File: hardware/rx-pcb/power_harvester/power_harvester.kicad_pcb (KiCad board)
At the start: 4 copper layers, 59 x 46.8 mm, 42 parts, among them J1 Conn_Coaxial_Small, J2 Conn_01x02_Pin, J3 Conn_Coaxial_Small, J4 Conn_Coaxial_Small

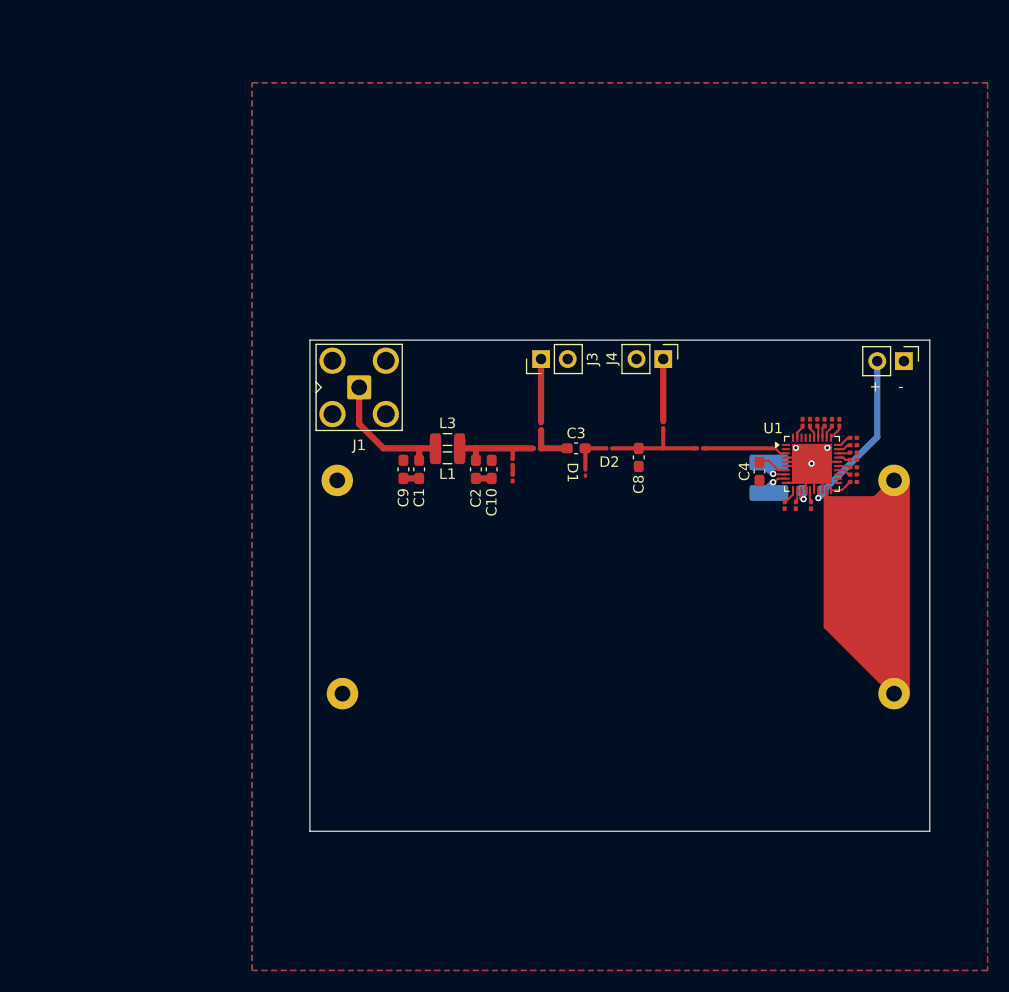
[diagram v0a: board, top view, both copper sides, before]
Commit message: fixed capacitance issue on harvester board
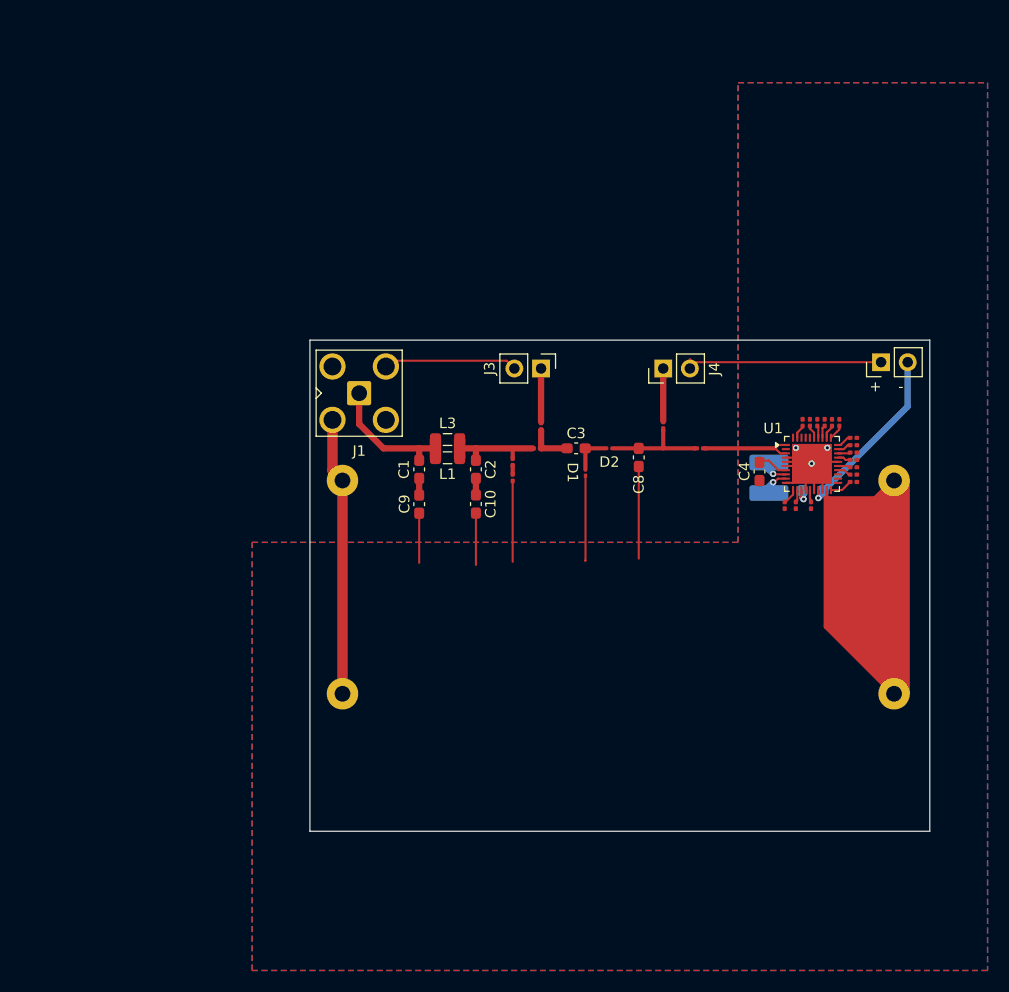
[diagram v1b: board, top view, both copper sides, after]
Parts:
- moved C9 3.64 mm to (106.9, 90.6), turned to -90 degrees
- moved C10 3.62 mm to (112.3, 90.6), turned to -90 degrees
- moved J2 2.18 mm to (150.9, 77.1), turned to 90 degrees
- moved J3 0.90 mm to (118.5, 77.7), turned to -90 degrees
- moved J4 0.90 mm to (130.1, 77.7), turned to 90 degrees
- moved J1 0.55 mm to (101.2, 80.0)
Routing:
- net GND: track 21.9 -> 114.0 mm
- net /Pin: track 7.96 -> 9.10 mm
- net /Po: track 16.3 -> 17.4 mm
- net Net-(J3-In): track 5.99 -> 5.02 mm
- net Net-(J4-In): track 5.89 -> 4.99 mm
- net Net-(J1-In): track 12.8 -> 12.2 mm

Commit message: harvester updates
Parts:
- added R21: x, Resistor_SMD:R_0805_2012Metric_Pad1.20x1.40mm_HandSolder, F.Cu at (152.2, 104.2)
- added R22: x, Resistor_SMD:R_0805_2012Metric_Pad1.20x1.40mm_HandSolder, F.Cu at (152.2, 100.5)
- added R23: x, Resistor_SMD:R_0805_2012Metric_Pad1.20x1.40mm_HandSolder, F.Cu at (152.2, 96.8)
- added R24: x, Resistor_SMD:R_0805_2012Metric_Pad1.20x1.40mm_HandSolder, F.Cu at (152.2, 93.0)
- added R25: x, Resistor_SMD:R_0805_2012Metric_Pad1.20x1.40mm_HandSolder, F.Cu at (139.2, 84.0)
- C1, C10, C2, C9: footprint Capacitor_SMD:C_0603_1608Metric_Pad1.08x0.95mm_HandSolder -> Capacitor_SMD:C_0402_1005Metric_Pad0.74x0.62mm_HandSolder
- moved C9 2.56 mm to (106.9, 88.0)
- moved C10 2.55 mm to (112.3, 88.0)
- moved R11 2.26 mm to (146.8, 90.2), turned to 90 degrees
- moved C2 1.45 mm to (112.3, 85.8)
- moved C1 1.43 mm to (106.9, 85.9)
- moved R19 0.72 mm to (118.5, 83.9)
- moved R14 0.51 mm to (148.8, 87.8)
- moved R4 0.51 mm to (148.8, 87.1)
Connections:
- U1 pad 2: unconnected-(U1-ZMPP-Pad2) -> Net-(U1-ZMPP)
- U1 pad 21: unconnected-(U1-ST_OVDIS-Pad21) -> Net-(U1-ST_OVDIS)
- U1 pad 22: unconnected-(U1-STO_RDY-Pad22) -> Net-(U1-STO_RDY)
- U1 pad 23: unconnected-(U1-STO_OVCH-Pad23) -> Net-(U1-STO_OVCH)
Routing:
- net Net-(U1-ST_OVDIS): track 0.00 -> 17.1 mm
- net /bank: track 49.5 -> 32.7 mm, vias 0 -> 1
- net Net-(U1-STO_RDY): track 0.00 -> 13.8 mm
- net Net-(U1-STO_OVCH): track 0.00 -> 10.6 mm
- net GND: track 114.0 -> 119.8 mm, vias 3 -> 5
- net /Pin: track 9.10 -> 13.0 mm, vias 0 -> 2
- net Net-(U1-ZMPP): track 0.00 -> 2.11 mm
- net Net-(C1-Pad2): track 1.59 -> 0.00 mm
- net Net-(U1-EN_STO_CH): track 2.15 -> 0.99 mm
- net Net-(J1-In): track 12.2 -> 11.1 mm
- net Net-(D3-K): track 9.04 -> 7.90 mm
- net Net-(C3-Pad1): track 3.90 -> 3.01 mm
- net Net-(U1-LOAD_CFG[1]): track 1.19 -> 1.70 mm
- net Net-(C10-Pad1): track 1.58 -> 1.06 mm

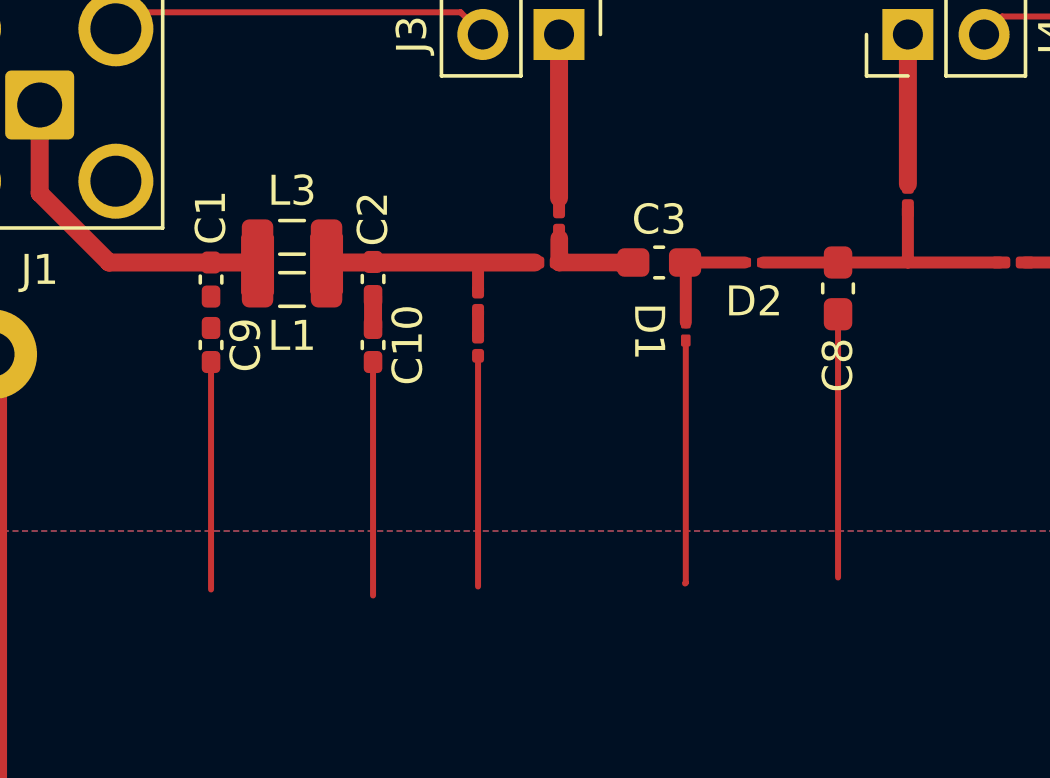
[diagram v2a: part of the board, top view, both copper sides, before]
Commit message: fixed capacitance issue on harvester board
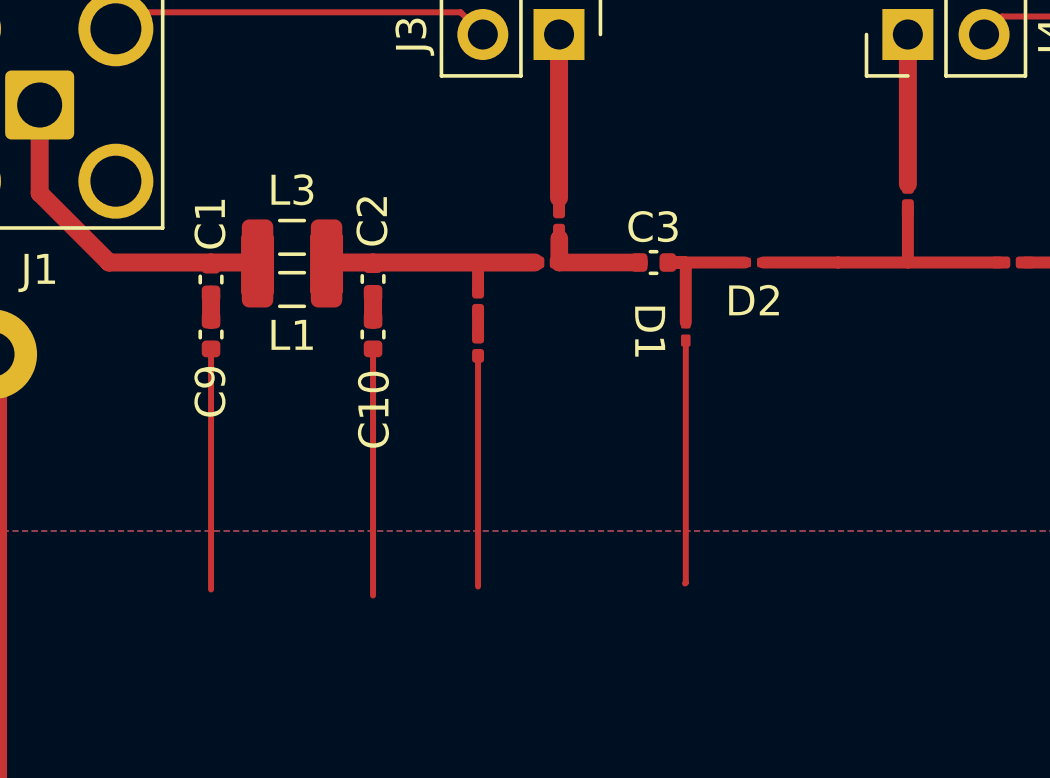
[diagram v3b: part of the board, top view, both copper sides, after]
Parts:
- removed C8: 22u, Capacitor_SMD:C_0603_1608Metric_Pad1.08x0.95mm_HandSolder
- C1, C10, C2, C9: footprint Capacitor_SMD:C_0402_1005Metric_Pad0.74x0.62mm_HandSolder -> Capacitor_SMD:C_0402_1005Metric
- C3: footprint Capacitor_SMD:C_0603_1608Metric_Pad1.08x0.95mm_HandSolder -> Capacitor_SMD:C_0402_1005Metric
- D1, D2: value D -> JDH2S02SL
- D3, D4: value D_Zener -> SP4340L-01WTG
- moved C10 0.35 mm to (112.3, 87.7)
- moved C9 0.35 mm to (106.9, 87.7)
- moved C3 0.19 mm to (121.7, 85.3)
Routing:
- net GND: track 119.8 -> 111.9 mm
- net Net-(D1-K): track 4.01 -> 5.15 mm
- net Net-(C1-Pad2): track 0.00 -> 0.85 mm
- removed copper zone on In1.Cu, net GND
- removed copper zone on In2.Cu, net GND
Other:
- copper layers 4 -> 2

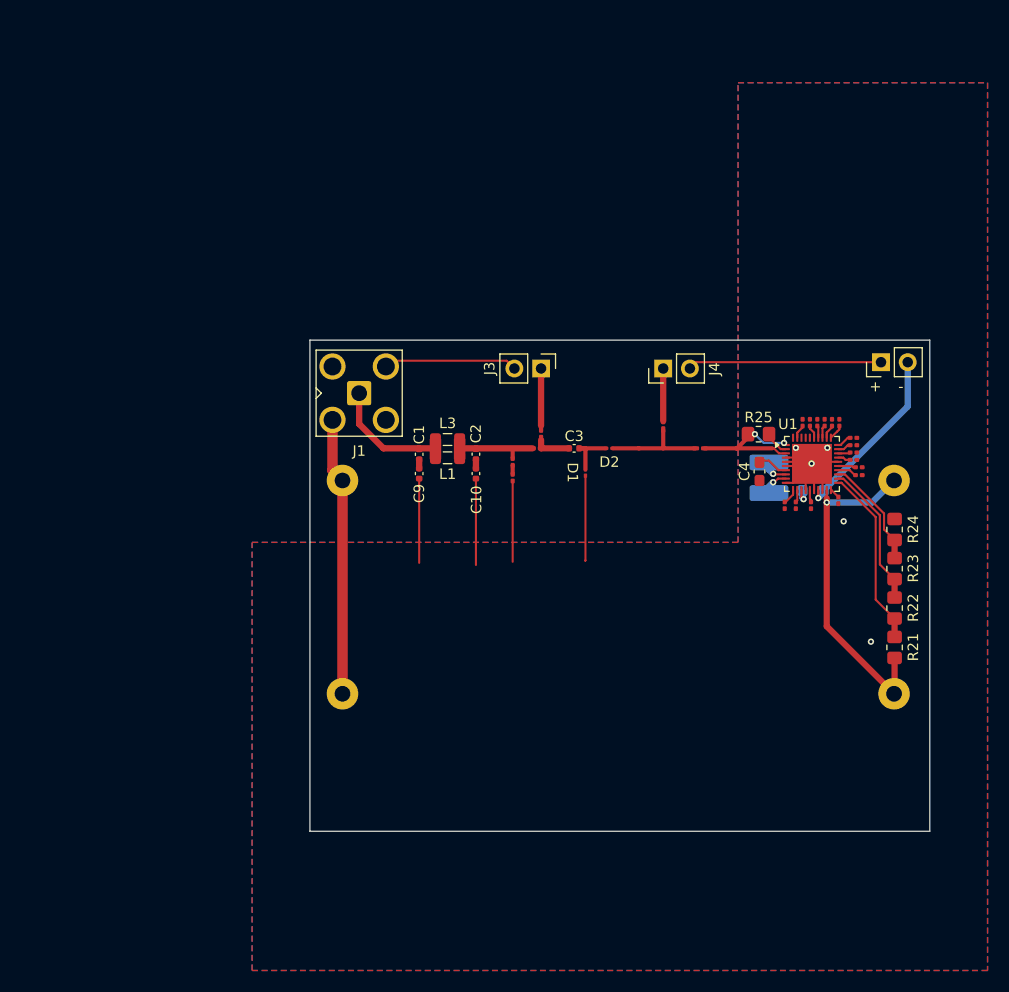
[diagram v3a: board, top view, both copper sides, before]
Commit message: double checked for purchase
updated TX SPI_CLK pin, was incorrect
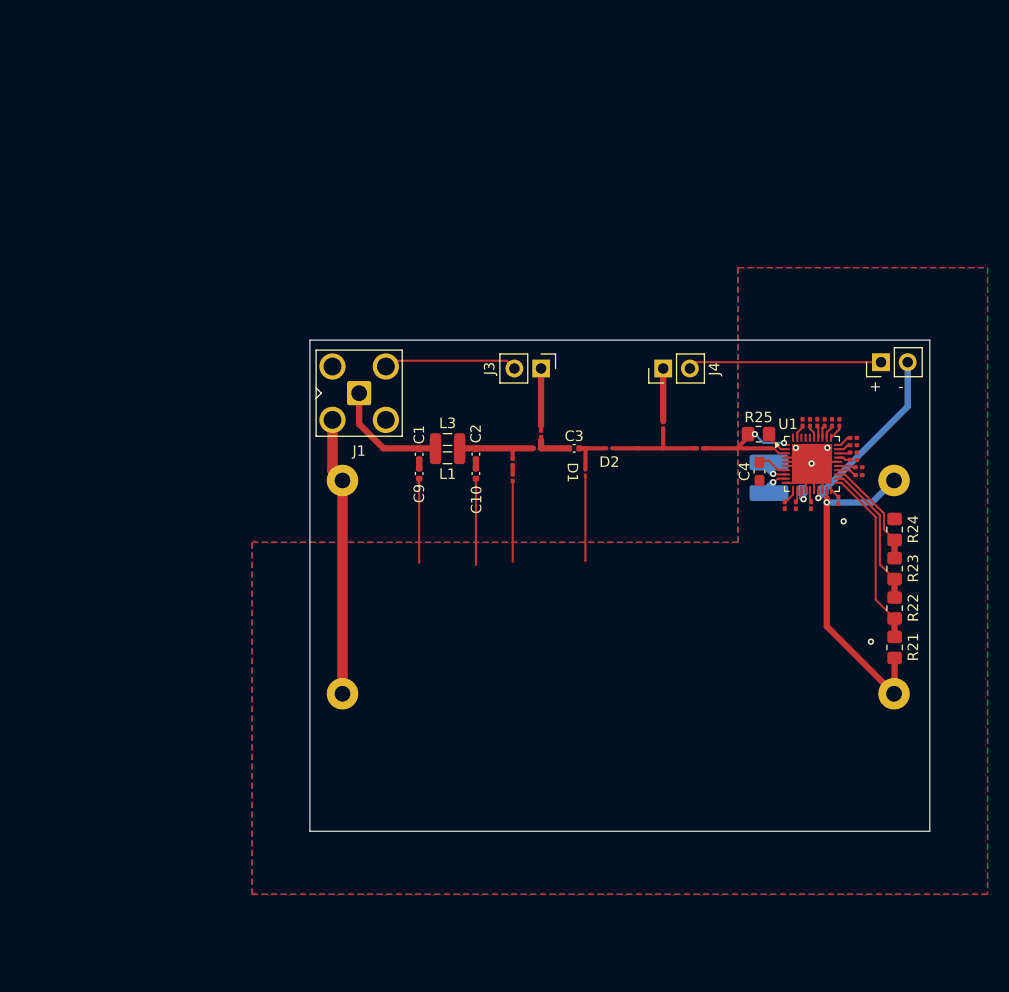
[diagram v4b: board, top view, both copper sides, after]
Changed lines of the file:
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@@
 		(capping no)
 		(filling no)
-		(zone_defaults)
 		(pcbplotparams
 			(layerselection 0x00000000_00000000_55555555_5755f5ff)
@@
 		(polygon
 			(pts
-				(xy 91 94.25) (xy 137.25 94.25) (xy 137.25 50.5) (xy 161 50.5) (xy 161 135) (xy 91 135)
+				(xy 91 94.25) (xy 137.25 94.25) (xy 137.25 68.1) (xy 161 68.1) (xy 161 127.75) (xy 91 127.75)
 			)
 		)

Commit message: updates for dr weeks
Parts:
- J3, J4: footprint Connector_PinHeader_2.54mm:PinHeader_1x02_P2.54mm_Vertical -> Connector_Coaxial:SMA_Molex_73251-2120_EdgeMount_Horizontal
- L1, L3: footprint Inductor_SMD:L_0805_2012Metric_Pad1.05x1.20mm_HandSolder -> Inductor_SMD:L_0402_1005Metric
- R12, R13, R8: value off -> on
- R2: value on -> off
- moved R15 1.81 mm to (149.1, 82.7)
- moved R8 1.81 mm to (141.8, 82.0)
- moved R9 1.47 mm to (149.1, 83.8)
- moved R2 1.39 mm to (143.0, 82.0)
- moved R1 1.16 mm to (149.1, 84.9)
- moved R11 1.15 mm to (146.8, 91.4)
- moved R13 1.10 mm to (144.1, 82.0)
- moved C10 1.01 mm to (111.3, 87.6)
- moved C2 1.01 mm to (111.3, 85.8)
- moved R20 1.00 mm to (130.1, 84.1)
- moved R10 0.99 mm to (147.4, 82.0)
- moved C1 0.95 mm to (107.8, 85.8)
- moved C9 0.95 mm to (107.8, 87.6)
- moved R3 0.93 mm to (149.1, 86.0)
- moved C4 0.91 mm to (139.4, 86.6), turned to 0 degrees
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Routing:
- net GND: track 111.9 -> 114.5 mm
- net Net-(U1-T_MPP[0]): track 1.42 -> 3.10 mm
- net Net-(J1-In): track 11.1 -> 12.7 mm
- net Net-(U1-STO_PRIO): track 1.30 -> 2.72 mm
- net Net-(U1-STO_CFG[2]): track 1.28 -> 2.60 mm
- net Net-(D3-K): track 7.90 -> 9.20 mm
- net Net-(U1-EN_HP): track 1.18 -> 2.35 mm
- net Net-(U1-EN_STO_CH): track 0.99 -> 2.14 mm
- net Net-(U1-STO_CFG[1]): track 1.16 -> 2.30 mm
- net Net-(D2-K): track 9.69 -> 8.57 mm
- net Net-(U1-EN_SLEEP): track 1.33 -> 2.42 mm
- net Net-(U1-EN_STO_FT): track 1.45 -> 2.52 mm
- net Net-(J4-In): track 4.99 -> 5.90 mm
- net Net-(U1-BUFSRC): track 2.89 -> 1.99 mm
- net Net-(U1-T_MPP[1]): track 1.33 -> 2.23 mm
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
